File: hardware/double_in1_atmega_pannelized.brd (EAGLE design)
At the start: 84 x 70 mm, 74 parts, among them IC1 MEGA8-AI, IC2 MEGA8-AI, J1 AVR-ISP-6PINAVR-ISP-6PIN-SMAL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, J2 AVR-ISP-6PINAVR-ISP-6PIN-SMAL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

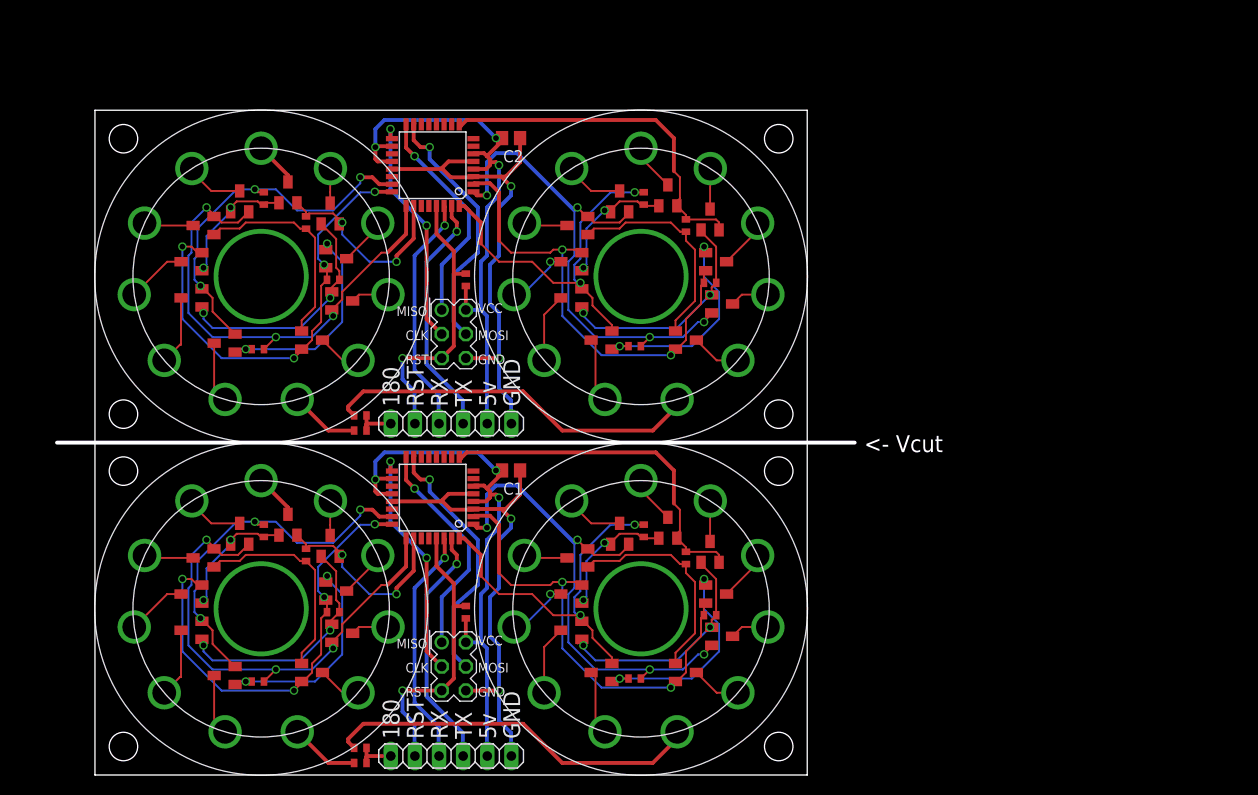
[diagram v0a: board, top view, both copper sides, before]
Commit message: [PCB] rev1; Change resistors size, center ATMEGA8, make slots for nixie alignment, minor changes
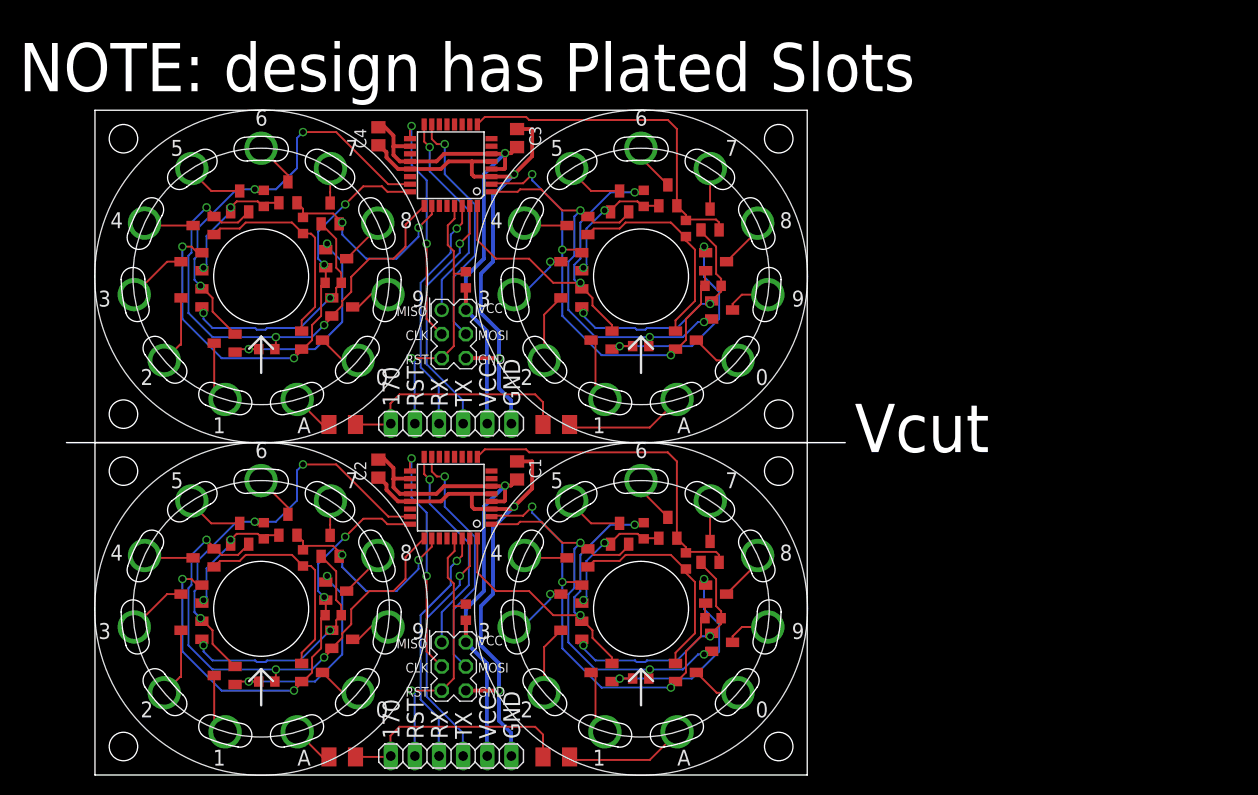
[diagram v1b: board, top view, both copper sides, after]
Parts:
- added C3, C4: (no value), eagle-ltspice:C0805
- R1, R11, R12, R13, R14, R15, R17, R18, R19, R2, R20, R22, R3, R4, R6, R7, R8, R9: device resistor:R0402 -> resistor:R0603
- R10, R16, R21, R5: device resistor:R0402 -> rcl:M1206
- U$1, U$2, U$3, U$4: device LC-516:LC-516 -> LC-516_play:LC-516
- moved C2 37.5 mm to (29.8, 32.3), turned to 90 degrees
- moved R10 20.7 mm to (48.6, 1.91), turned to 180 degrees
- moved R21 20.7 mm to (48.6, 36.9), turned to 180 degrees
- moved R5 2.01 mm to (26.0, 1.91)
- moved R16 2.01 mm to (26.0, 36.9)
- moved IC1 1.91 mm to (37.5, 29.2)
- moved IC2 1.91 mm to (37.5, 64.2)
- moved R15 0.95 mm to (18.1, 44.8)
- moved R4 0.95 mm to (18.1, 9.84)
- moved C1 0.64 mm to (44.5, 32.1), turned to 270 degrees
- moved T13 0.63 mm to (66.0, 14.0)
- moved T4 0.63 mm to (26.0, 14.3)
- moved R20 0.63 mm to (57.5, 45.2)
- moved R9 0.63 mm to (57.5, 10.2)
- moved T23 0.63 mm to (26.0, 49.3)
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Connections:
- net GND: now also C2.1
- net GND1: now also C3.1, C4.1; no longer C2.1
- net VCC: now also C2.2
- net VCC1: now also C3.2, C4.2; no longer C2.2
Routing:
- net N$1: track 40.0 -> 12.7 mm
- net N$7: track 40.0 -> 12.7 mm
- net +15V: track 4.84 -> 25.1 mm
- net +15V1: track 4.84 -> 25.1 mm
- net TSB8: track 53.7 -> 45.6 mm, vias 4 -> 3
- net TSB4: track 53.7 -> 45.6 mm, vias 4 -> 3
- net GND: track 52.4 -> 59.4 mm
- net GND1: track 52.4 -> 59.4 mm
- net VCC: track 62.0 -> 56.3 mm, vias 3 -> 1
- net VCC1: track 62.0 -> 56.3 mm, vias 3 -> 1
- net TSA5: track 39.7 -> 45.2 mm
- net TSA2: track 39.7 -> 45.2 mm
- net TSA8: track 48.2 -> 51.6 mm
- net TSA1: track 48.2 -> 51.6 mm
- net N$4: track 7.35 -> 4.43 mm
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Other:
- board size 84 x 70 mm -> 82 x 70 mm
- board text added: "170"
- board text added: "C1"
- board text added: "C2"
- board text added: "NOTE: design has Plated Slots"
- board text added: "Vcut"
- board text removed: "180"
- board text removed: "5v"
- board text removed: "<- Vcut"
- board text removed: "Flayols - Bailly 12/17"

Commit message: generate gerber for jlpcb
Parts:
- added GOLD_ORB_SM1, GOLD_ORB_SM2: OSHWLOGOLOGO5MM, oshw:OSHW_5MM
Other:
- board size 82 x 70 mm -> 75 x 70 mm
- board text added: "hackaday.io/project/69708 T Flayols - 2018"
- board text removed: "C1"
- board text removed: "C2"
- board text removed: "NOTE: design has Plated Slots"
- board text removed: "Vcut"
